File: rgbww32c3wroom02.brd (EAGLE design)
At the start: 36.8 x 20.3 mm, 21 parts, among them IC2 7805TV

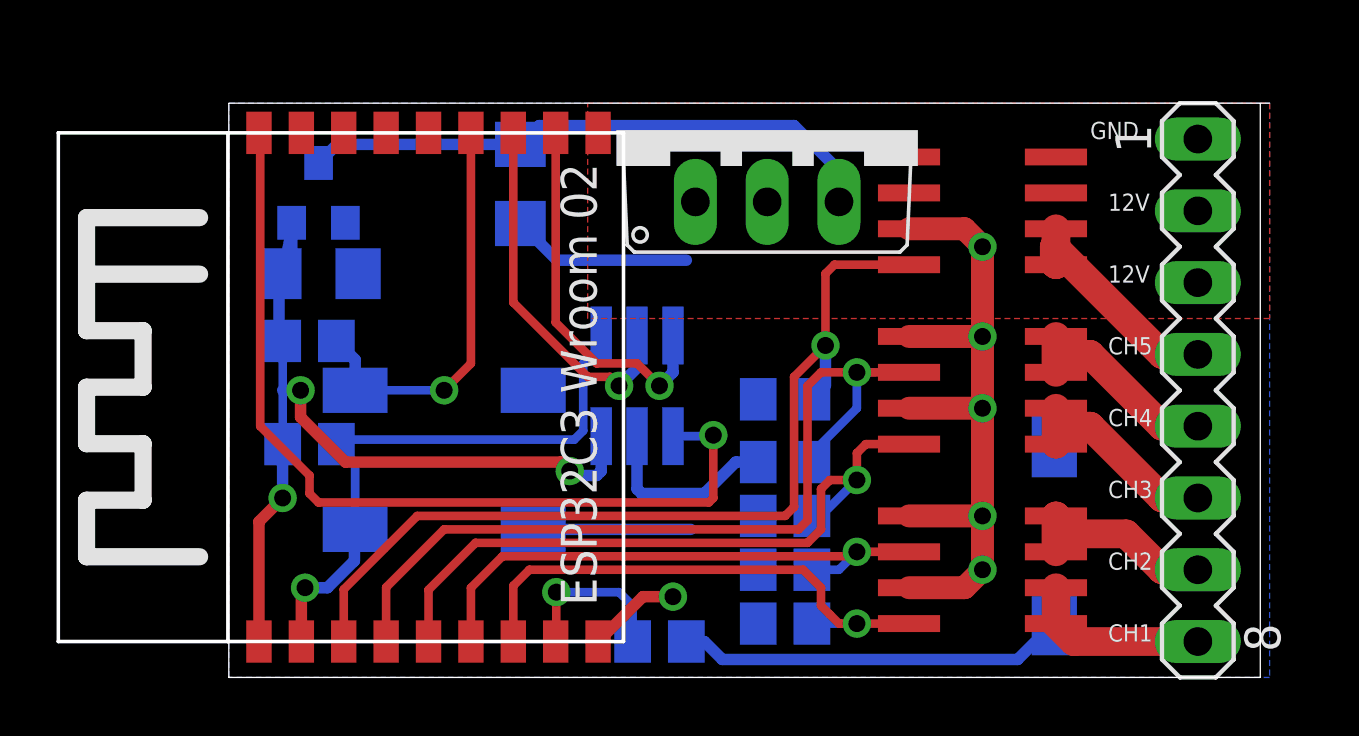
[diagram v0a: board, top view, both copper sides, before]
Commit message: moved the 3.3V reg to clean up things a bit. Not sure if it will be in the way of the 5V VRs inductance
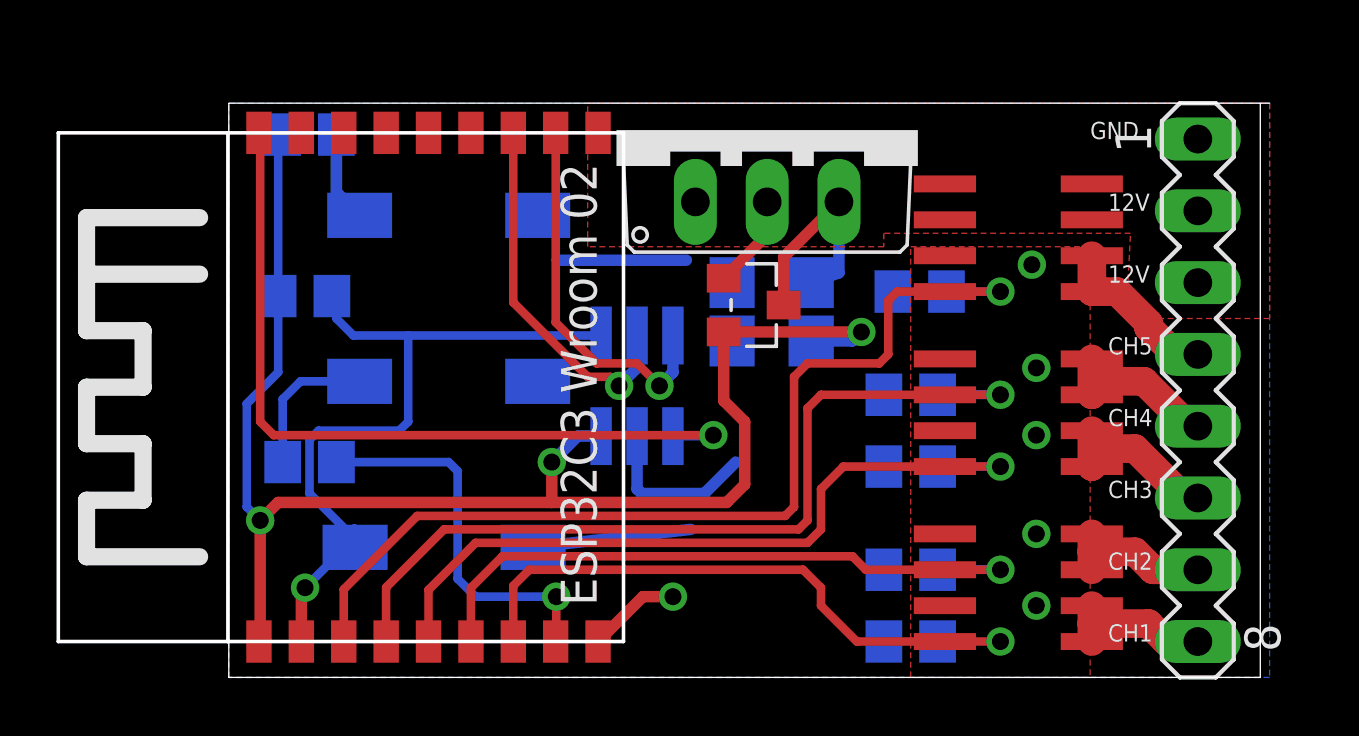
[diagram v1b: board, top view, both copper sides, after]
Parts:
- moved PRG 22.1 mm to (7.78, 70.2), turned to 0 degrees
- moved C1 16.2 mm to (19.2, 71.6), turned to 0 degrees
- moved U$4 15.9 mm to (18.6, 72.9), flipped to the top, turned to 270 degrees
- moved R7 13.9 mm to (2.86, 67.3), turned to 180 degrees
- moved C2 9.55 mm to (19.2, 73.7), turned to 0 degrees
- moved R10 7.30 mm to (2.86, 78.9)
- moved CLR 6.19 mm to (7.78, 76.0)
- moved R1 6.10 mm to (24.4, 73.3)
- moved R6 5.24 mm to (2.70, 73.2)
- moved R5 5.04 mm to (24.1, 69.7)
- moved R2 4.78 mm to (24.1, 67.2)
- moved R4 4.49 mm to (24.1, 61.0)
- moved R3 4.45 mm to (24.1, 63.5)
- moved U$3 1.59 mm to (27.9, 75.2)
- moved U$2 1.50 mm to (27.9, 69.1)
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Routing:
- net GND: track 46.9 -> 22.7 mm
- net 3V3: track 31.4 -> 52.4 mm
- net 5V: track 20.7 -> 8.01 mm
- net CLR: track 14.7 -> 3.20 mm, vias 1 -> 0
- net PRG1: track 13.8 -> 5.21 mm
- net PRG: track 5.92 -> 13.6 mm
- net EN: track 21.1 -> 27.1 mm
- net GPIO0: track 31.6 -> 27.9 mm
- net CH2S: track 19.8 -> 23.5 mm
- net CH5S: track 32.2 -> 35.2 mm
- net CH5: track 8.59 -> 6.03 mm
- net CH3S: track 24.5 -> 26.9 mm
- net CH1S: track 19.0 -> 20.9 mm
- net CH2: track 7.08 -> 5.28 mm
- net CH3: track 7.61 -> 6.01 mm
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- added copper zone on layer 1, net GND

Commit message: some corrections before production
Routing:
- net CLR: track 3.20 -> 13.5 mm, vias 0 -> 1
- net GND: track 22.7 -> 18.6 mm
- net CH1S: track 20.9 -> 23.4 mm
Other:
- outline, holes or cut-outs redrawn
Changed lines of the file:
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@@
 <board>
 <plain>
-<wire x1="0" y1="59.69" x2="36.5" y2="59.69" width="0" layer="20"/>
-<wire x1="36.5" y1="59.69" x2="36.5" y2="80" width="0" layer="20"/>
+<wire x1="0" y1="59.69" x2="36.8175" y2="59.69" width="0" layer="20"/>
+<wire x1="36.8175" y1="59.69" x2="36.8175" y2="80" width="0" layer="20"/>
 <wire x1="0" y1="80" x2="0" y2="59.69" width="0" layer="20"/>
 <wire x1="34.29" y1="76.2" x2="36.83" y2="76.2" width="1.524" layer="17"/>
@@
 <wire x1="34.29" y1="63.5" x2="36.83" y2="63.5" width="1.6764" layer="29"/>
 <wire x1="34.29" y1="60.96" x2="36.83" y2="60.96" width="1.6764" layer="29"/>
-<text x="30.48" y="78.74" size="0.6096" layer="25">GND</text>
-<text x="31.115" y="76.2" size="0.6096" layer="25">12V</text>
-<text x="31.115" y="73.66" size="0.6096" layer="25">12V</text>
-<text x="31.115" y="60.96" size="0.6096" layer="25">CH1</text>
-<text x="31.115" y="63.5" size="0.6096" layer="25">CH2</text>
-<text x="31.115" y="66.04" size="0.6096" layer="25">CH3</text>
-<text x="31.115" y="68.58" size="0.6096" layer="25">CH4</text>
-<text x="31.115" y="71.12" size="0.6096" layer="25">CH5</text>
+<text x="29.5275" y="79.0575" size="0.6096" layer="25">GND</text>
+<text x="31.90875" y="76.99375" size="0.6096" layer="25">12V</text>
+<text x="31.90875" y="74.6125" size="0.6096" layer="25">12V</text>
+<text x="32.0675" y="61.9125" size="0.6096" layer="25">CH1</text>
+<text x="32.0675" y="64.29375" size="0.6096" layer="25">CH2</text>
+<text x="32.0675" y="66.9925" size="0.6096" layer="25">CH3</text>
+<text x="32.0675" y="69.5325" size="0.6096" layer="25">CH4</text>
+<text x="31.90875" y="72.0725" size="0.6096" layer="25">CH5</text>
 <wire x1="0.01" y1="80.01" x2="36.83" y2="80.01" width="0" layer="20"/>
 <text x="15.5575" y="64.92875" size="0.6096" layer="26" rot="MR90">G0</text>
@@
 <element name="PRG" library="SparkFun-Electromechanical" package="TACTILE-SWITCH-1101NE" value="" x="7.77875" y="70.1675" smashed="yes" rot="MR0">
 <attribute name="PROD_ID" value="SWCH-00815" x="7.77875" y="70.1675" size="1.778" layer="28" rot="MR0" display="off"/>
-<attribute name="NAME" x="6.65125" y="67.24625" size="0.762" layer="26" rot="MR0"/>
+<attribute name="NAME" x="10.46125" y="72.32625" size="0.762" layer="26" rot="MR0"/>
 <attribute name="VALUE" x="10.77875" y="67.4675" size="0.762" layer="28" rot="MR0"/>
 </element>
@@
 <via x="28.575" y="64.77" extent="1-16" drill="0.6"/>
 <via x="28.575" y="62.23" extent="1-16" drill="0.6"/>
-<polygon width="0.3048" layer="16">
-<vertex x="0" y="80.01"/>
-<vertex x="36.83" y="80.01"/>
-<vertex x="36.83" y="59.69"/>
-<vertex x="0" y="59.69"/>
-</polygon>
 <contactref element="RST" pad="1"/>
 <contactref element="SV1" pad="1"/>
@@
 <contactref element="PRG" pad="1"/>
 <contactref element="U$5" pad="P$1"/>
-<wire x1="14.44625" y1="68.22875" x2="14.44625" y2="66.3575" width="0.4064" layer="16"/>
-<wire x1="14.44625" y1="66.3575" x2="14.605" y2="66.19875" width="0.4064" layer="16"/>
-<wire x1="14.605" y1="66.19875" x2="16.8275" y2="66.19875" width="0.4064" layer="16"/>
-<wire x1="16.8275" y1="66.19875" x2="17.93875" y2="67.31" width="0.4064" layer="16"/>
-<via x="15.71625" y="62.5475" extent="1-16" drill="0.6"/>
-<wire x1="13.0675" y1="60.96" x2="14.655" y2="62.5475" width="0.4064" layer="1"/>
-<wire x1="14.655" y1="62.5475" x2="15.71625" y2="62.5475" width="0.4064" layer="1"/>
+<via x="14.44625" y="61.2775" extent="1-16" drill="0.6"/>
+<wire x1="13.0675" y1="60.96" x2="13.385" y2="61.2775" width="0.4064" layer="1"/>
+<wire x1="13.385" y1="61.2775" x2="14.44625" y2="61.2775" width="0.4064" layer="1"/>
 <wire x1="11.6175" y1="74.45375" x2="16.1925" y2="74.45375" width="0.4064" layer="16"/>
-<wire x1="10.77" y1="64.29375" x2="16.35125" y2="64.92875" width="0.4064" layer="16"/>
 <wire x1="17.51375" y1="73.81625" x2="19.05" y2="75.3525" width="0.4064" layer="1"/>
 <wire x1="19.05" y1="75.3525" x2="19.05" y2="76.5175" width="0.4064" layer="1"/>
@@
 <vertex x="30.48" y="59.69"/>
 </polygon>
+<polygon width="0.4064" layer="16">
+<vertex x="0" y="59.69"/>
+<vertex x="0" y="80.01"/>
+<vertex x="36.83" y="80.01"/>
+<vertex x="36.83" y="59.69"/>
+</polygon>
+<wire x1="25.4" y1="74.6125" x2="27.14625" y2="74.6125" width="0.6096" layer="1"/>
+<wire x1="25.4" y1="70.96125" x2="27.14625" y2="70.96125" width="0.6096" layer="1"/>
+<wire x1="25.4" y1="68.42125" x2="27.305" y2="68.42125" width="0.6096" layer="1"/>
+<wire x1="25.4" y1="64.77" x2="27.305" y2="64.77" width="0.6096" layer="1"/>
+<wire x1="25.4" y1="62.23" x2="27.305" y2="62.23" width="0.6096" layer="1"/>
 </signal>
 <signal name="CH1">
@@
 <wire x1="4.62875" y1="76.04125" x2="3.8075" y2="76.8625" width="0.4064" layer="16"/>
 <wire x1="3.8075" y1="76.8625" x2="3.8075" y2="78.89875" width="0.4064" layer="16"/>
-<wire x1="3.8075" y1="78.89875" x2="8.5675" y2="78.96" width="0" layer="19" extent="1-16"/>
+<wire x1="8.5675" y1="78.96" x2="8.5675" y2="77.94125" width="0.3048" layer="1"/>
+<wire x1="8.5675" y1="77.94125" x2="8.255" y2="77.62875" width="0.3048" layer="1"/>
+<wire x1="8.255" y1="77.62875" x2="3.01625" y2="77.62875" width="0.3048" layer="1"/>
+<wire x1="3.01625" y1="77.62875" x2="2.69875" y2="77.31125" width="0.3048" layer="1"/>
+<via x="2.69875" y="77.31125" extent="1-16" drill="0.6"/>
+<wire x1="2.69875" y1="77.31125" x2="2.69875" y2="76.2" width="0.3048" layer="16"/>
+<wire x1="2.69875" y1="76.2" x2="2.8575" y2="76.04125" width="0.3048" layer="16"/>
+<wire x1="2.8575" y1="76.04125" x2="4.62875" y2="76.04125" width="0.3048" layer="16"/>
 </signal>
 <signal name="12V">
@@
 <wire x1="17.51375" y1="69.48125" x2="18.25625" y2="68.73875" width="0.4064" layer="1"/>
 <wire x1="18.25625" y1="68.73875" x2="18.25625" y2="66.51625" width="0.4064" layer="1"/>
-<wire x1="18.25625" y1="66.51625" x2="17.62125" y2="65.88125" width="0.4064" layer="1"/>
-<wire x1="17.62125" y1="65.88125" x2="11.43" y2="65.88125" width="0.4064" layer="1"/>
-<wire x1="11.43" y1="65.88125" x2="1.74625" y2="65.88125" width="0.4064" layer="1"/>
+<wire x1="18.25625" y1="66.51625" x2="17.78" y2="66.04" width="0.4064" layer="1"/>
+<wire x1="17.78" y1="66.04" x2="11.43" y2="66.04" width="0.4064" layer="1"/>
+<wire x1="11.43" y1="66.04" x2="1.905" y2="66.04" width="0.4064" layer="1"/>
 <wire x1="13.17625" y1="68.22875" x2="12.34875" y2="68.22875" width="0.4064" layer="16"/>
 <wire x1="12.34875" y1="68.22875" x2="11.43" y2="67.31" width="0.4064" layer="16"/>
 <via x="11.43" y="67.31" extent="1-16" drill="0.6"/>
-<wire x1="11.43" y1="67.31" x2="11.43" y2="65.88125" width="0.4064" layer="1"/>
-<wire x1="1.74625" y1="65.88125" x2="1.11125" y2="65.24625" width="0.4064" layer="1"/>
+<wire x1="11.43" y1="67.31" x2="11.43" y2="66.04" width="0.4064" layer="1"/>
+<wire x1="1.905" y1="66.04" x2="1.11125" y2="65.24625" width="0.4064" layer="1"/>
 <wire x1="1.11125" y1="65.24625" x2="1.11125" y2="61.00375" width="0.4064" layer="1"/>
 <wire x1="1.11125" y1="61.00375" x2="1.0675" y2="60.96" width="0.4064" layer="1"/>
@@
 <wire x1="4.445" y1="64.90375" x2="4.1525" y2="64.90375" width="0.3048" layer="16"/>
 <wire x1="4.1525" y1="64.90375" x2="2.8575" y2="66.19875" width="0.3048" layer="16"/>
-<wire x1="2.8575" y1="66.19875" x2="2.8575" y2="68.10375" width="0.3048" layer="16"/>
-<wire x1="2.8575" y1="68.10375" x2="3.175" y2="68.42125" width="0.3048" layer="16"/>
-<wire x1="3.175" y1="68.42125" x2="6.0325" y2="68.42125" width="0.3048" layer="16"/>
+<wire x1="2.8575" y1="66.19875" x2="2.8575" y2="68.2625" width="0.3048" layer="16"/>
+<wire x1="2.8575" y1="68.2625" x2="3.01625" y2="68.42125" width="0.3048" layer="16"/>
+<wire x1="3.01625" y1="68.42125" x2="6.0325" y2="68.42125" width="0.3048" layer="16"/>
 <wire x1="6.0325" y1="68.42125" x2="6.35" y2="68.73875" width="0.3048" layer="16"/>
 <wire x1="6.35" y1="68.73875" x2="6.35" y2="71.78875" width="0.3048" layer="16"/>
@@
 <wire x1="10.63625" y1="63.5" x2="20.32" y2="63.5" width="0.3048" layer="1"/>
 <wire x1="20.32" y1="63.5" x2="20.955" y2="62.865" width="0.3048" layer="1"/>
-<wire x1="20.955" y1="62.865" x2="20.955" y2="62.23" width="0.3048" layer="1"/>
+<wire x1="20.955" y1="62.865" x2="20.955" y2="61.595" width="0.3048" layer="1"/>
 <wire x1="25.34" y1="60.96" x2="22.225" y2="60.96" width="0.3048" layer="1"/>
-<wire x1="22.225" y1="60.96" x2="20.955" y2="62.23" width="0.3048" layer="1"/>
+<wire x1="22.225" y1="60.96" x2="20.955" y2="61.595" width="0.3048" layer="1"/>
 <wire x1="27.305" y1="60.96" x2="25.34" y2="60.96" width="0.3048" layer="1"/>
-<wire x1="25.34" y1="60.96" x2="25.08" y2="60.96" width="0" layer="19" extent="1-16"/>
+<wire x1="25.08" y1="60.96" x2="27.305" y2="60.96" width="0.3048" layer="16"/>
 </signal>
 <signal name="CH2S">
@@
 <contactref element="SV1" pad="4"/>
 <wire x1="30.54" y1="73.3425" x2="30.54" y2="74.6125" width="1.016" layer="1"/>
-<wire x1="30.54" y1="73.3425" x2="31.4325" y2="73.3425" width="1.016" layer="1"/>
-<wire x1="31.4325" y1="73.3425" x2="32.54375" y2="72.23125" width="1.016" layer="1"/>
-<wire x1="32.54375" y1="72.23125" x2="32.54375" y2="72.0725" width="1.016" layer="1"/>
-<wire x1="32.54375" y1="72.0725" x2="33.49625" y2="71.12" width="1.016" layer="1"/>
+<wire x1="30.54" y1="73.3425" x2="31.27375" y2="72.23125" width="1.016" layer="1"/>
+<wire x1="31.27375" y1="72.23125" x2="32.385" y2="72.23125" width="1.016" layer="1"/>
+<wire x1="32.385" y1="72.23125" x2="33.49625" y2="71.12" width="1.016" layer="1"/>
 <wire x1="33.49625" y1="71.12" x2="34.29" y2="71.12" width="1.016" layer="1"/>
 </signal>

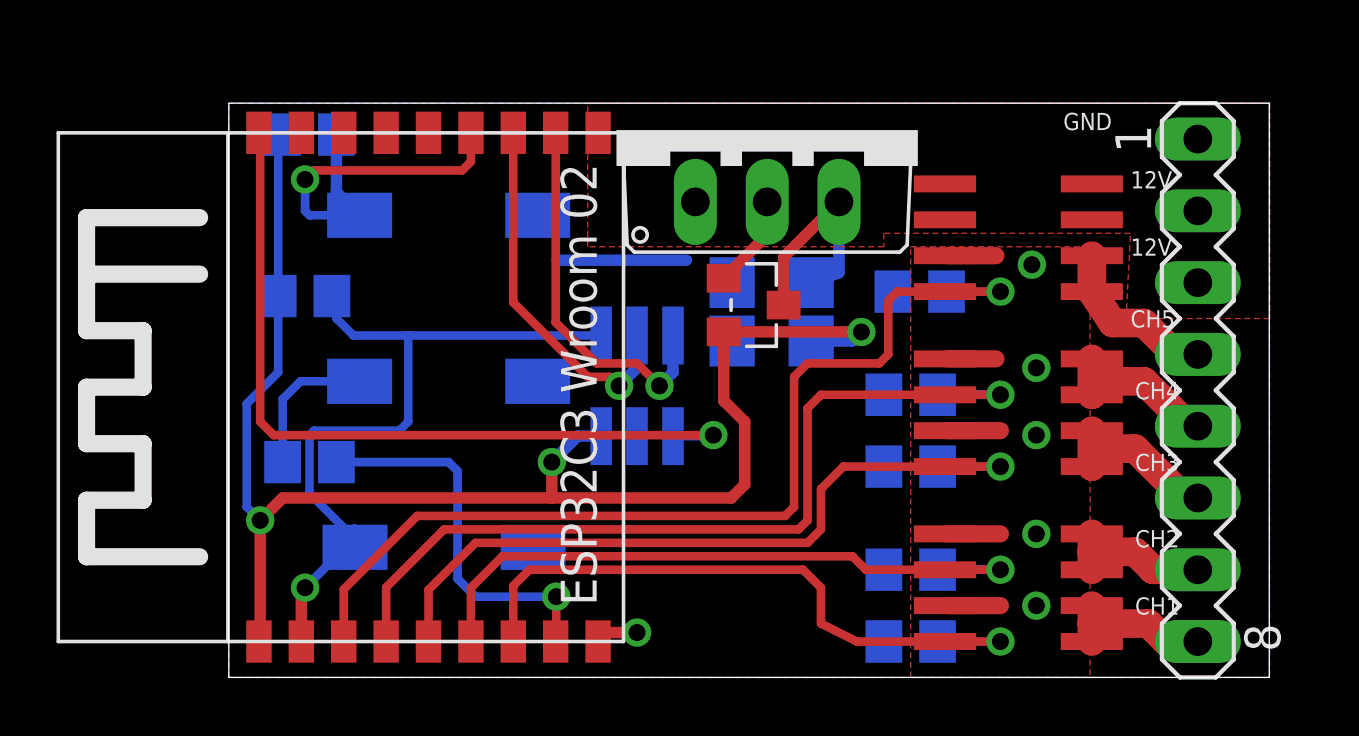
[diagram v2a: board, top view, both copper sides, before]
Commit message: added local switching voltage regulator
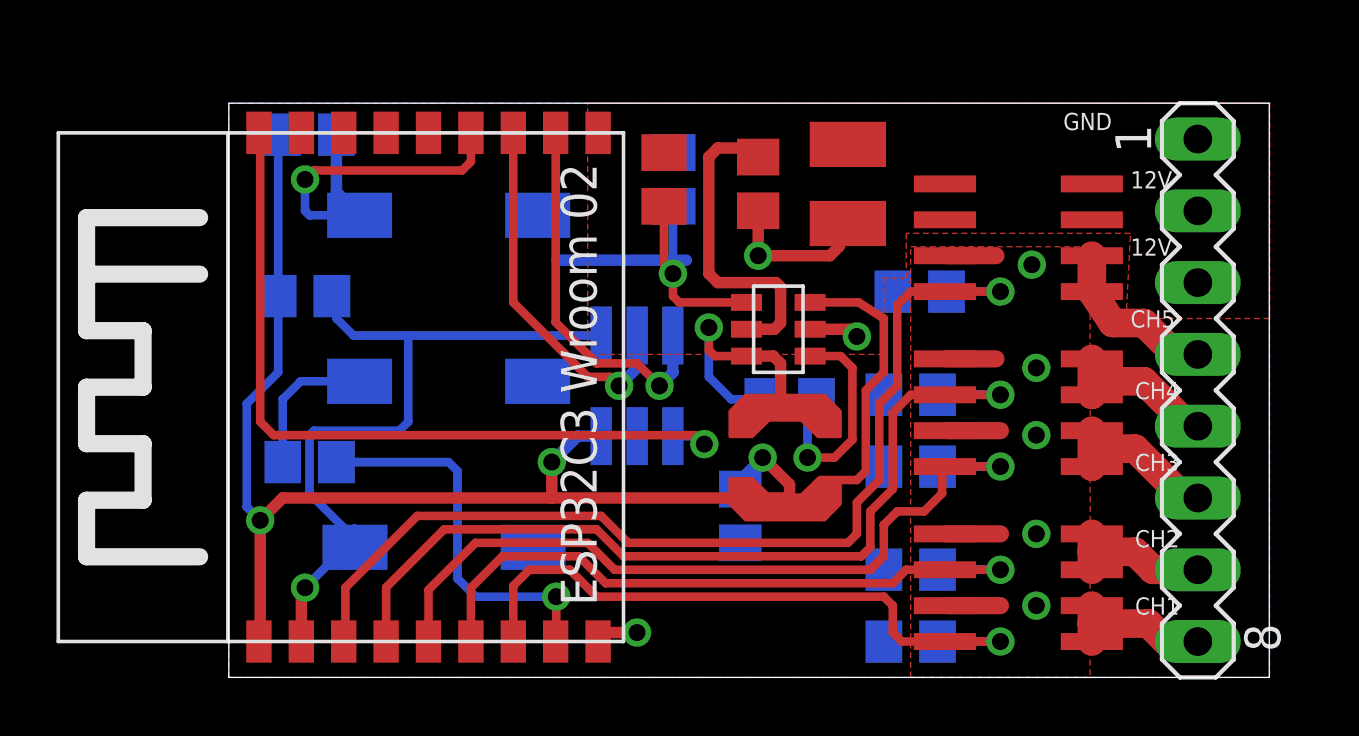
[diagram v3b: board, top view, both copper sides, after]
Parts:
- removed C1, C2: (no value), rcl:C1206
- removed IC2: 7805TV, linear:TO220V
- removed U$4: MCP1700, MCP1700:SOT-23
- added C3: 4.7µF, rcl:C1210
- added C4, C6: 100nF, rcl:C0805
- added C5: 22µF, rcl:C0805
- added L1: 15µH, TI_Components:LPS4018
- added R8: 412kOhm, rcl:M0805
- added R9: 200kOhm, rcl:M0805
- added U$6: TPS5604030, TI_Components:SOT23-6
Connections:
- removed net 5V: C2.1, IC2.3, U$4.3
- new net BOOT: C6.1, U$6.1
- new net EN_P: R8.1, R9.2, U$6.4
- new net SW: C6.2, L1.1, U$6.6
- net 12V: now also C3.1, C4.1, R8.2, U$6.5; no longer IC2.1
- net 3V3: now also C5.1, L1.2, U$6.3; no longer C1.1, U$4.2
- net GND: now also C3.2, C4.2, C5.2, R9.1, U$6.2; no longer C1.2, C2.2, IC2.2, U$4.1
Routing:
- net 12V: track 0.00 -> 11.6 mm
- net SW: track 0.00 -> 9.01 mm, vias 0 -> 1
- net EN_P: track 0.00 -> 8.39 mm, vias 0 -> 1
- net BOOT: track 0.00 -> 8.25 mm, vias 0 -> 1
- net 5V: track 8.01 -> 0.00 mm
- net 3V3: track 52.2 -> 56.4 mm
- net GND: track 18.6 -> 22.5 mm, vias 6 -> 8
- net CH3S: track 26.9 -> 28.0 mm
- net CH5S: track 35.2 -> 36.0 mm
- net CH4S: track 31.0 -> 31.8 mm
